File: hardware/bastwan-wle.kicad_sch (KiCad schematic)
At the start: 33 parts, among them J1 USB_C, J2 Conn_Right, J3 Conn_Left, J4 Conn_Battery, J5 SWD, Q1 DMG3415U-7, SW1 RST, U1 RAK3172, U2 MCP1700_DFN6, U3 CP2104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

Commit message: fix Serial programming
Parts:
- C9: value 10uF -> 4.7uF
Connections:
- net +3V3: now also U3.5 (VIO), U3.7 (REGIN)
- net D+: now also U3.3 (D+)
- net D-: now also U3.4 (D-)
- net GND: now also U3.2 (GND), U3.25 (GND)
- net RX: now also U1.5 (PB7_UART1_RX); no longer U1.1 (PA3_UART2_RX)
- net RX_USB: now also U1.2 (PA2_UART2_TX), U3.20 (RXD); no longer U1.4 (PB6_UART1_TX)
- net TX: now also U1.4 (PB6_UART1_TX); no longer U1.2 (PA2_UART2_TX)
- net TX_USB: now also U1.1 (PA3_UART2_RX), U3.21 (TXD); no longer U1.5 (PB7_UART1_RX)
- net VBUS: now also U3.8 (VBUS)
- net at U3.16 (VPP): now also C9.1
- no-connect marks 19 -> 20
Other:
- moved on the sheet: C1, C7, C8, C9, U3

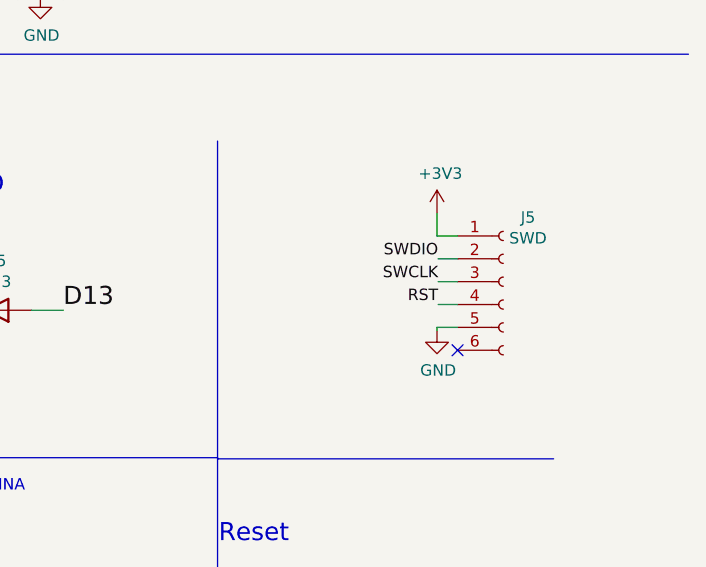
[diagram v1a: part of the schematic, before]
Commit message: Fix SWD connector
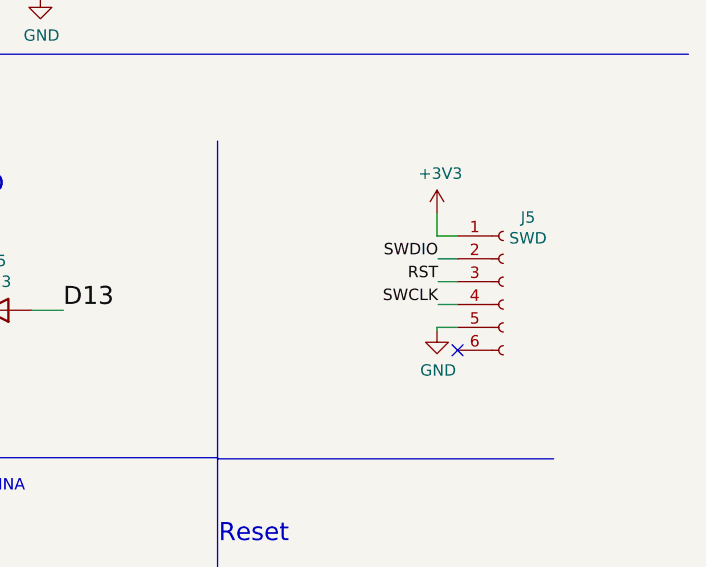
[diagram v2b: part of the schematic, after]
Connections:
- net RST: now also J5.3 (Pin_3); no longer J5.4 (Pin_4)
- net SWCLK: now also J5.4 (Pin_4); no longer J5.3 (Pin_3)
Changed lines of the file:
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@@
     (effects (font (size 1.27 1.27)) (justify left bottom))
   )
-  (label "SWCLK" (at 248.539 113.03 180)
+  (label "RST" (at 248.539 113.03 180)
     (effects (font (size 1.27 1.27)) (justify right bottom))
   )
@@
     (effects (font (size 1.27 1.27)) (justify right bottom))
   )
-  (label "RST" (at 248.539 115.57 180)
+  (label "SWCLK" (at 248.539 115.57 180)
     (effects (font (size 1.27 1.27)) (justify right bottom))
   )

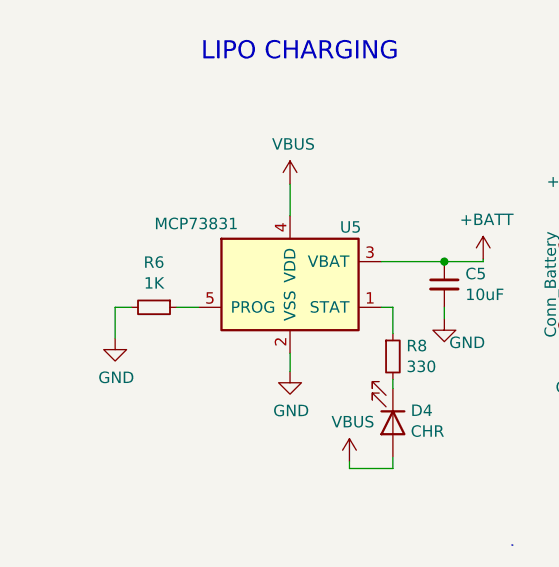
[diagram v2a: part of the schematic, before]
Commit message: fix resistor charger
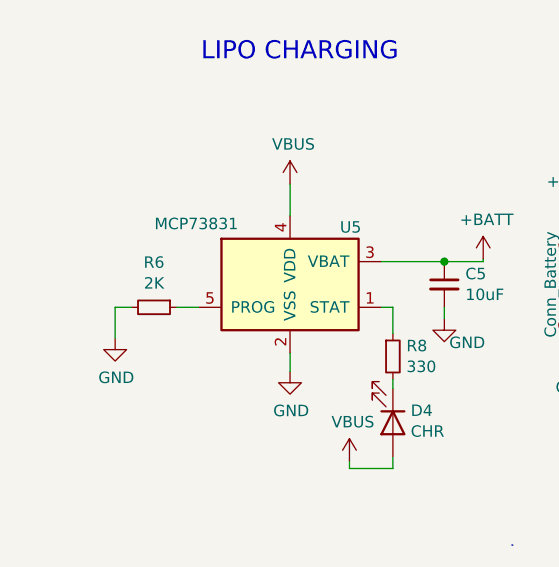
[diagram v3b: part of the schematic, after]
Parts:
- R6: value 1K -> 2K; #LCSC C384295 -> C25590; manf# WR06X102JTL -> WR06X1001FTL
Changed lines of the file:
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@@
     (in_bom yes) (on_board yes)
     (property "Reference" "R6" (id 0) (at 21.082 167.3606 90))
-    (property "Value" "1K" (id 1) (at 21.082 169.672 90))
+    (property "Value" "2K" (id 1) (at 21.082 169.672 90))
     (property "Footprint" "Resistor_SMD:R_0603_1608Metric" (id 2) (at 21.082 172.339 0)
       (effects (font (size 1.27 1.27)) hide)
     )
-    (property "Datasheet" "https://datasheet.lcsc.com/lcsc/1912111437_Walsin-Tech-Corp-WR06X102JTL_C384295.pdf" (id 3) (at 21.082 172.339 0)
-      (effects (font (size 1.27 1.27)) hide)
-    )
-    (property "manf#" "WR06X102JTL" (id 4) (at -151.003 150.876 0)
-      (effects (font (size 1.27 1.27)) hide)
-    )
-    (property "#LCSC" "C384295" (id 5) (at 21.082 172.339 0)
+    (property "Datasheet" "https://datasheet.lcsc.com/lcsc/2206010100_UNI-ROYAL-Uniroyal-Elec-0603WAJ0202T5E_C25590.pdf" (id 3) (at 21.082 172.339 0)
+      (effects (font (size 0 0)) hide)
+    )
+    (property "manf#" "WR06X1001FTL" (id 4) (at -151.003 150.876 0)
+      (effects (font (size 1.27 1.27)) hide)
+    )
+    (property "#LCSC" "C25590" (id 5) (at 21.082 172.339 0)
       (effects (font (size 1.27 1.27)) hide)
     )
@@
     )
     (path "/00000000-0000-0000-0000-00005dd5d374"
-      (reference "R6") (unit 1) (value "1K") (footprint "Resistor_SMD:R_0603_1608Metric")
+      (reference "R6") (unit 1) (value "2K") (footprint "Resistor_SMD:R_0603_1608Metric")
     )
     (path "/00000000-0000-0000-0000-00005dd44c55"
